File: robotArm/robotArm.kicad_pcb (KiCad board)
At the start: 4 copper layers, 127.6 x 90.2 mm, 51 parts, among them J1 Barrel_Jack, J2 ENDSTOP INPUTS, J3 STEPPER1, J4 STEPPER4, J5 STEPPER2, J6 STEPPER3, J7 Conn_01x04_Pin, J8 Screw_Terminal_01x02, J9 END EFFECTOR, SW1 SW_DIP_x08, U2 TMC2209_SILENTSTEPSTICK, U3 74HC245, U4 TMC2209_MODULE, U5 TMC2209 Module, U6 74HC165, U9 74LS279

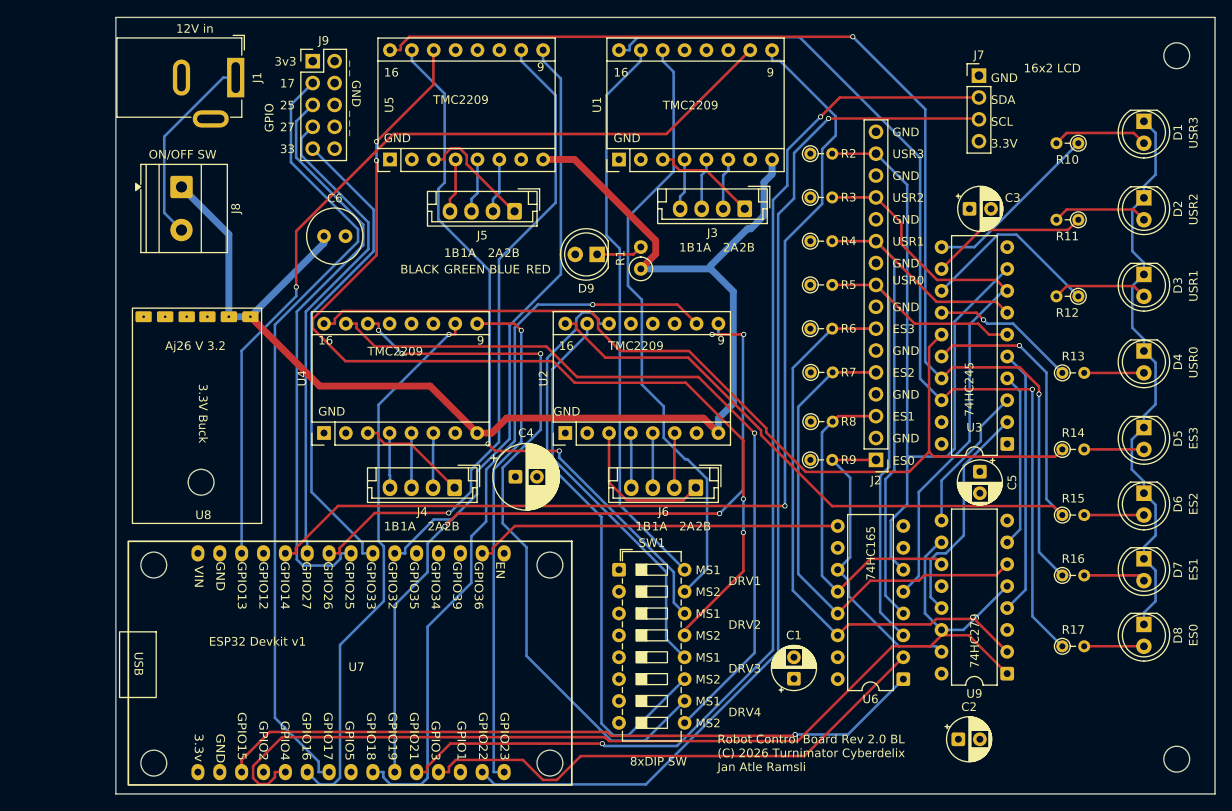
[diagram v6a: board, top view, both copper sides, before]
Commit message: Fixed trace width
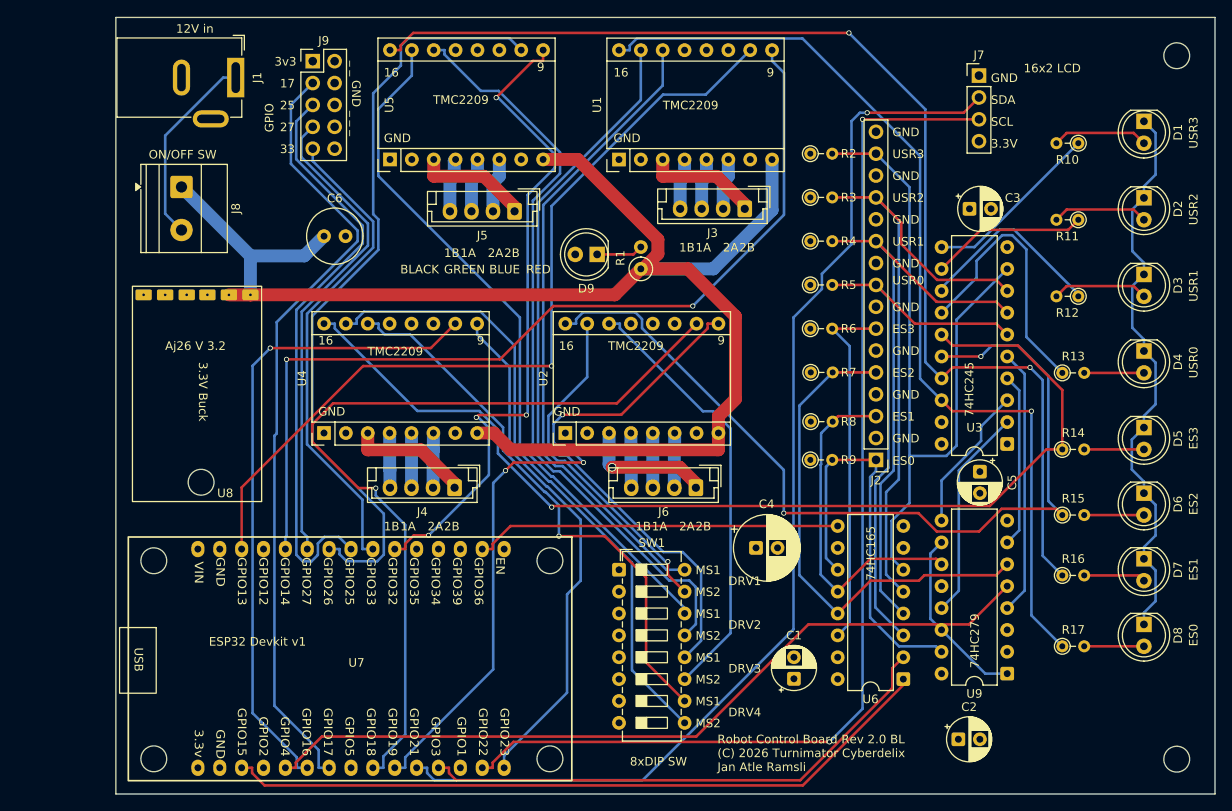
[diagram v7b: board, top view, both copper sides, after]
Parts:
- moved C4 29.1 mm to (111.2, 106.7)
- moved U8 2.54 mm to (53.8, 101.3)
- moved U7 0.50 mm to (63.4, 118.7)
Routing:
- net MS2-DRV2: track 118.8 -> 87.5 mm, vias 4 -> 0
- net /Endstop Section/ES3: track 66.8 -> 42.1 mm
- net MS1-DRV4: track 84.4 -> 64.7 mm, vias 3 -> 1
- net +12V: track 160.0 -> 178.3 mm
- net MS2-DRV3: track 68.9 -> 50.8 mm
- net MS2-DRV4: track 90.0 -> 74.2 mm, vias 1 -> 0
- net Net-(U3-B4): track 16.9 -> 31.5 mm, vias 1 -> 0
- net DIR_1: track 119.6 -> 106.5 mm, vias 1 -> 2
- net STEP_2: track 76.8 -> 89.8 mm, vias 1 -> 0
- net /EN_DRV4: track 111.1 -> 122.9 mm, vias 0 -> 1
- net STEP_4: track 63.9 -> 75.6 mm
- net /Endstop Section/ES0: track 36.4 -> 47.2 mm
- net DIR_3: track 91.1 -> 80.9 mm, vias 4 -> 3
- net /RESET_DRV: track 124.7 -> 114.5 mm
- net STEP_3: track 87.2 -> 97.3 mm
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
